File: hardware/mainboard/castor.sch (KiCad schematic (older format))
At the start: 42 parts, among them Q1 MMBT3906, U3 TL074, U4 74LVC2G74, U5 MCP6001-OT, U6 TL074

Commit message: hardware: assign new MPNs for mainboard BOM
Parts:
- C11, C12, C13: Reqs audio path, 25v -> audio path, 20v; finalized yes -> yes & alt; mpn alt (none) -> CL21A106KAFN3NE
- C14, C15, C16, C17: Reqs audio filter, 25v -> audio filter, 20v
- C9: finalized yes -> yes & alt; mpn alt GRM1885C1H102FA01D -> GRM1885C1H102FA01*
- R10, R11, R12: mpn alts 2 (none) -> RT0603DRD0747KL
- R13, R14, R15, R2, R6: mpn RR0816P-103-D -> RG1608P-103-D-T5; mpn alt ERA-3AED103V -> RR0816P-103-D; mpn alts 2 (none) -> ERA-3AED103V
- U5: mpn alt (none) -> AD8541ARTZ
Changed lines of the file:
@@
 F 3 "~" H 2500 1400 50  0001 C CNN
 F 4 "yes" H 2500 1400 50  0001 C CNN "finalized"
-F 5 "RR0816P-103-D" H 2500 1400 50  0001 C CNN "mpn"
+F 5 "RG1608P-103-D-T5" H 2500 1400 50  0001 C CNN "mpn"
 F 6 "1%, 15mW, control path" H 2500 1400 50  0001 C CNN "Reqs"
 F 7 "62mW, 0.5%" H 2500 1400 50  0001 C CNN "mpn specs"
-F 8 "ERA-3AED103V" H 2500 1400 50  0001 C CNN "mpn alt"
+F 8 "RR0816P-103-D" H 2500 1400 50  0001 C CNN "mpn alt"
+F 9 "ERA-3AED103V" H 2500 1400 50  0001 C CNN "mpn alts 2"
 	1    2500 1400
 	-1   0    0    1
@@
 F 3 "~" H 3300 2500 50  0001 C CNN
 F 4 "C0G 1%, 25v, ramp core" H 3300 2500 50  0001 C CNN "Reqs"
-F 5 "yes" H 3300 2500 50  0001 C CNN "finalized"
+F 5 "yes & alt" H 3300 2500 50  0001 C CNN "finalized"
 F 6 "GRM1885C1H102FA01J" H 3300 2500 50  0001 C CNN "mpn"
 F 7 "1%, 50v" H 3300 2500 50  0001 C CNN "mpn specs"
-F 8 "GRM1885C1H102FA01D" H 3300 2500 50  0001 C CNN "mpn alt"
+F 8 "GRM1885C1H102FA01*" H 3300 2500 50  0001 C CNN "mpn alt"
 	1    3300 2500
 	0    1    1    0
@@
 F 3 "~" H 4850 2550 50  0001 C CNN
 F 4 "yes" H 4850 2550 50  0001 C CNN "finalized"
-F 5 "RR0816P-103-D" H 4850 2550 50  0001 C CNN "mpn"
+F 5 "RG1608P-103-D-T5" H 4850 2550 50  0001 C CNN "mpn"
 F 6 "1%, 15mW, audio path" H 4850 2550 50  0001 C CNN "Reqs"
 F 7 "62mW, 0.5%" H 4850 2550 50  0001 C CNN "mpn specs"
-F 8 "ERA-3AED103V" H 4850 2550 50  0001 C CNN "mpn alt"
+F 8 "RR0816P-103-D" H 4850 2550 50  0001 C CNN "mpn alt"
+F 9 "ERA-3AED103V" H 4850 2550 50  0001 C CNN "mpn alts 2"
 	1    4850 2550
 	0    -1   -1   0
@@
 F 2 "Capacitor_SMD:C_0805_2012Metric_Pad1.15x1.40mm_HandSolder" H 7988 1400 50  0001 C CNN
 F 3 "~" H 7950 1550 50  0001 C CNN
-F 4 "yes" H 7950 1550 50  0001 C CNN "finalized"
+F 4 "yes & alt" H 7950 1550 50  0001 C CNN "finalized"
 F 5 "CL21A106KAYNNN" H 7950 1550 50  0001 C CNN "mpn"
 F 6 "10% 25v" H 7950 1550 50  0001 C CNN "mpn specs"
-F 7 "" H 7950 1550 50  0001 C CNN "mpn alt"
-F 8 "audio path, 25v" H 7950 1550 50  0001 C CNN "Reqs"
+F 7 "CL21A106KAFN3NE" H 7950 1550 50  0001 C CNN "mpn alt"
+F 8 "audio path, 20v" H 7950 1550 50  0001 C CNN "Reqs"
 	1    7950 1550
 	0    1    1    0
@@
 F 3 "~" H 8350 1550 50  0001 C CNN
 F 4 "yes" H 8350 1550 50  0001 C CNN "finalized"
-F 5 "RR0816P-103-D" H 8350 1550 50  0001 C CNN "mpn"
+F 5 "RG1608P-103-D-T5" H 8350 1550 50  0001 C CNN "mpn"
 F 6 "1%, 15mW, audio path" H 8350 1550 50  0001 C CNN "Reqs"
 F 7 "62mW, 0.5%" H 8350 1550 50  0001 C CNN "mpn specs"
-F 8 "ERA-3AED103V" H 8350 1550 50  0001 C CNN "mpn alt"
+F 8 "RR0816P-103-D" H 8350 1550 50  0001 C CNN "mpn alt"
+F 9 "ERA-3AED103V" H 8350 1550 50  0001 C CNN "mpn alts 2"
 	1    8350 1550
 	0    -1   -1   0
@@
 F 7 "62mW, 0.5%" H 8150 1700 50  0001 C CNN "mpn specs"
 F 8 "ERA-3AED473V" H 8150 1700 50  0001 C CNN "mpn alt"
+F 9 "RT0603DRD0747KL" H 8150 1700 50  0001 C CNN "mpn alts 2"
 	1    8150 1700
 	1    0    0    -1
@@
 F 6 "5% 50v" H 8850 1000 50  0001 C CNN "mpn specs"
 F 7 "GCM1885C2A220JA16J" H 8850 1000 50  0001 C CNN "mpn alt"
-F 8 "audio filter, 25v" H 8850 1000 50  0001 C CNN "Reqs"
+F 8 "audio filter, 20v" H 8850 1000 50  0001 C CNN "Reqs"
 	1    8850 1000
 	0    1    1    0
@@
 F 2 "Capacitor_SMD:C_0805_2012Metric_Pad1.15x1.40mm_HandSolder" H 7988 2550 50  0001 C CNN
 F 3 "~" H 7950 2700 50  0001 C CNN
-F 4 "yes" H 7950 2700 50  0001 C CNN "finalized"
+F 4 "yes & alt" H 7950 2700 50  0001 C CNN "finalized"
 F 5 "CL21A106KAYNNN" H 7950 2700 50  0001 C CNN "mpn"
 F 6 "10% 25v" H 7950 2700 50  0001 C CNN "mpn specs"
-F 7 "" H 7950 2700 50  0001 C CNN "mpn alt"
-F 8 "audio path, 25v" H 7950 2700 50  0001 C CNN "Reqs"
+F 7 "CL21A106KAFN3NE" H 7950 2700 50  0001 C CNN "mpn alt"
+F 8 "audio path, 20v" H 7950 2700 50  0001 C CNN "Reqs"
 	1    7950 2700
 	0    1    1    0
@@
 F 3 "~" H 8350 2700 50  0001 C CNN
 F 4 "yes" H 8350 2700 50  0001 C CNN "finalized"
-F 5 "RR0816P-103-D" H 8350 2700 50  0001 C CNN "mpn"
+F 5 "RG1608P-103-D-T5" H 8350 2700 50  0001 C CNN "mpn"
 F 6 "1%, 15mW, audio path" H 8350 2700 50  0001 C CNN "Reqs"
 F 7 "62mW, 0.5%" H 8350 2700 50  0001 C CNN "mpn specs"
-F 8 "ERA-3AED103V" H 8350 2700 50  0001 C CNN "mpn alt"
+F 8 "RR0816P-103-D" H 8350 2700 50  0001 C CNN "mpn alt"
+F 9 "ERA-3AED103V" H 8350 2700 50  0001 C CNN "mpn alts 2"
 	1    8350 2700
 	0    -1   -1   0
@@
 F 7 "62mW, 0.5%" H 8150 2850 50  0001 C CNN "mpn specs"
 F 8 "ERA-3AED473V" H 8150 2850 50  0001 C CNN "mpn alt"
+F 9 "RT0603DRD0747KL" H 8150 2850 50  0001 C CNN "mpn alts 2"
 	1    8150 2850
 	1    0    0    -1
@@
 F 6 "5% 50v" H 8850 2150 50  0001 C CNN "mpn specs"
 F 7 "GCM1885C2A220JA16J" H 8850 2150 50  0001 C CNN "mpn alt"
-F 8 "audio filter, 25v" H 8850 2150 50  0001 C CNN "Reqs"
+F 8 "audio filter, 20v" H 8850 2150 50  0001 C CNN "Reqs"
 	1    8850 2150
 	0    1    1    0
@@
 F 5 "VJ0603A8R2DXACW1BC" H 8850 4900 50  0001 C CNN "mpn"
 F 6 "25v" H 8850 4900 50  0001 C CNN "mpn specs"
-F 7 "audio filter, 25v" H 8850 4900 50  0001 C CNN "Reqs"
+F 7 "audio filter, 20v" H 8850 4900 50  0001 C CNN "Reqs"
 F 8 "GRM1885C1H8R2WA01D" H 8850 4900 50  0001 C CNN "mpn alt"
 	1    8850 4900
@@
 F 4 "yes" H 2100 5350 50  0001 C CNN "finalized"
 F 5 "MCP6001T-I/OT" H 2100 5350 50  0001 C CNN "mpn"
+F 6 "AD8541ARTZ" H 2100 5350 50  0001 C CNN "mpn alt"
 	1    2100 5350
 	1    0    0    1
@@
 F 6 "5% 50v" H 8850 3300 50  0001 C CNN "mpn specs"
 F 7 "GCM1885C2A220JA16J" H 8850 3300 50  0001 C CNN "mpn alt"
-F 8 "audio filter, 25v" H 8850 3300 50  0001 C CNN "Reqs"
+F 8 "audio filter, 20v" H 8850 3300 50  0001 C CNN "Reqs"
 	1    8850 3300
 	0    1    1    0
@@
 F 7 "62mW, 0.5%" H 8150 4000 50  0001 C CNN "mpn specs"
 F 8 "ERA-3AED473V" H 8150 4000 50  0001 C CNN "mpn alt"
+F 9 "RT0603DRD0747KL" H 8150 4000 50  0001 C CNN "mpn alts 2"
 	1    8150 4000
 	1    0    0    -1
@@
 F 3 "~" H 8350 3850 50  0001 C CNN
 F 4 "yes" H 8350 3850 50  0001 C CNN "finalized"
-F 5 "RR0816P-103-D" H 8350 3850 50  0001 C CNN "mpn"
+F 5 "RG1608P-103-D-T5" H 8350 3850 50  0001 C CNN "mpn"
 F 6 "1%, 15mW, audio path" H 8350 3850 50  0001 C CNN "Reqs"
 F 7 "62mW, 0.5%" H 8350 3850 50  0001 C CNN "mpn specs"
-F 8 "ERA-3AED103V" H 8350 3850 50  0001 C CNN "mpn alt"
+F 8 "RR0816P-103-D" H 8350 3850 50  0001 C CNN "mpn alt"
+F 9 "ERA-3AED103V" H 8350 3850 50  0001 C CNN "mpn alts 2"
 	1    8350 3850
 	0    -1   -1   0
@@
 F 2 "Capacitor_SMD:C_0805_2012Metric_Pad1.15x1.40mm_HandSolder" H 7988 3700 50  0001 C CNN
 F 3 "~" H 7950 3850 50  0001 C CNN
-F 4 "yes" H 7950 3850 50  0001 C CNN "finalized"
+F 4 "yes & alt" H 7950 3850 50  0001 C CNN "finalized"
 F 5 "CL21A106KAYNNN" H 7950 3850 50  0001 C CNN "mpn"
 F 6 "10% 25v" H 7950 3850 50  0001 C CNN "mpn specs"
-F 7 "" H 7950 3850 50  0001 C CNN "mpn alt"
-F 8 "audio path, 25v" H 7950 3850 50  0001 C CNN "Reqs"
+F 7 "CL21A106KAFN3NE" H 7950 3850 50  0001 C CNN "mpn alt"
+F 8 "audio path, 20v" H 7950 3850 50  0001 C CNN "Reqs"
 	1    7950 3850
 	0    1    1    0

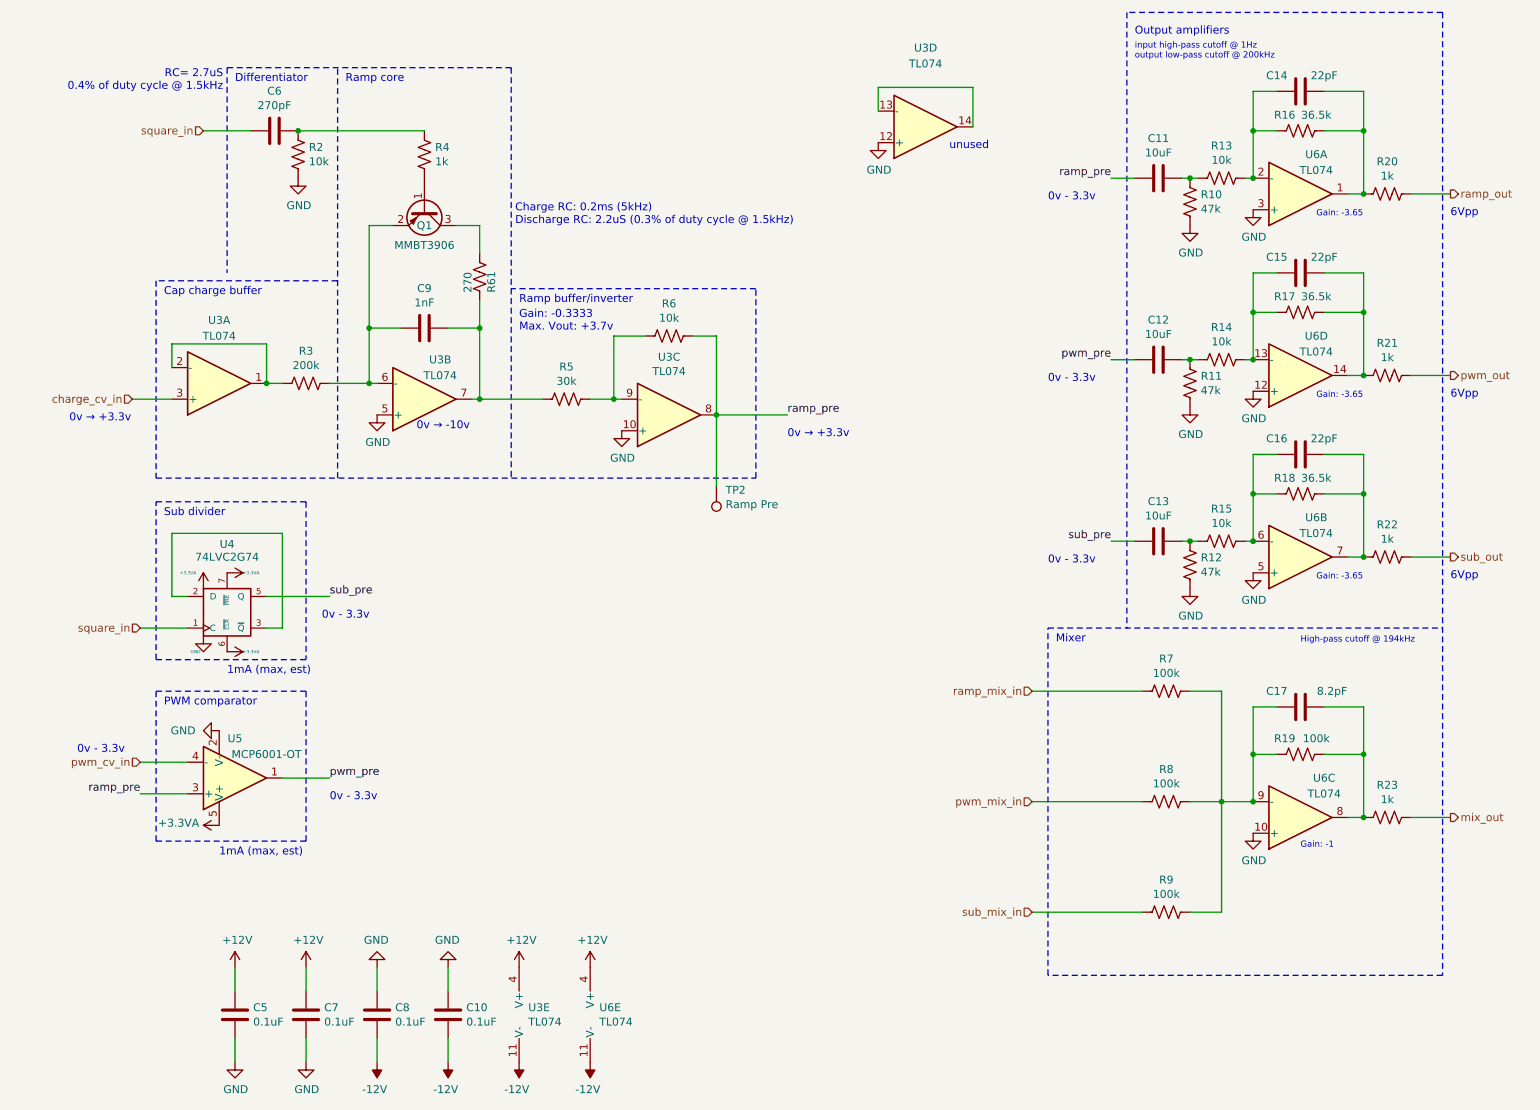
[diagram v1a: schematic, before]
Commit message: hardware: mark version 4 of the mainboard
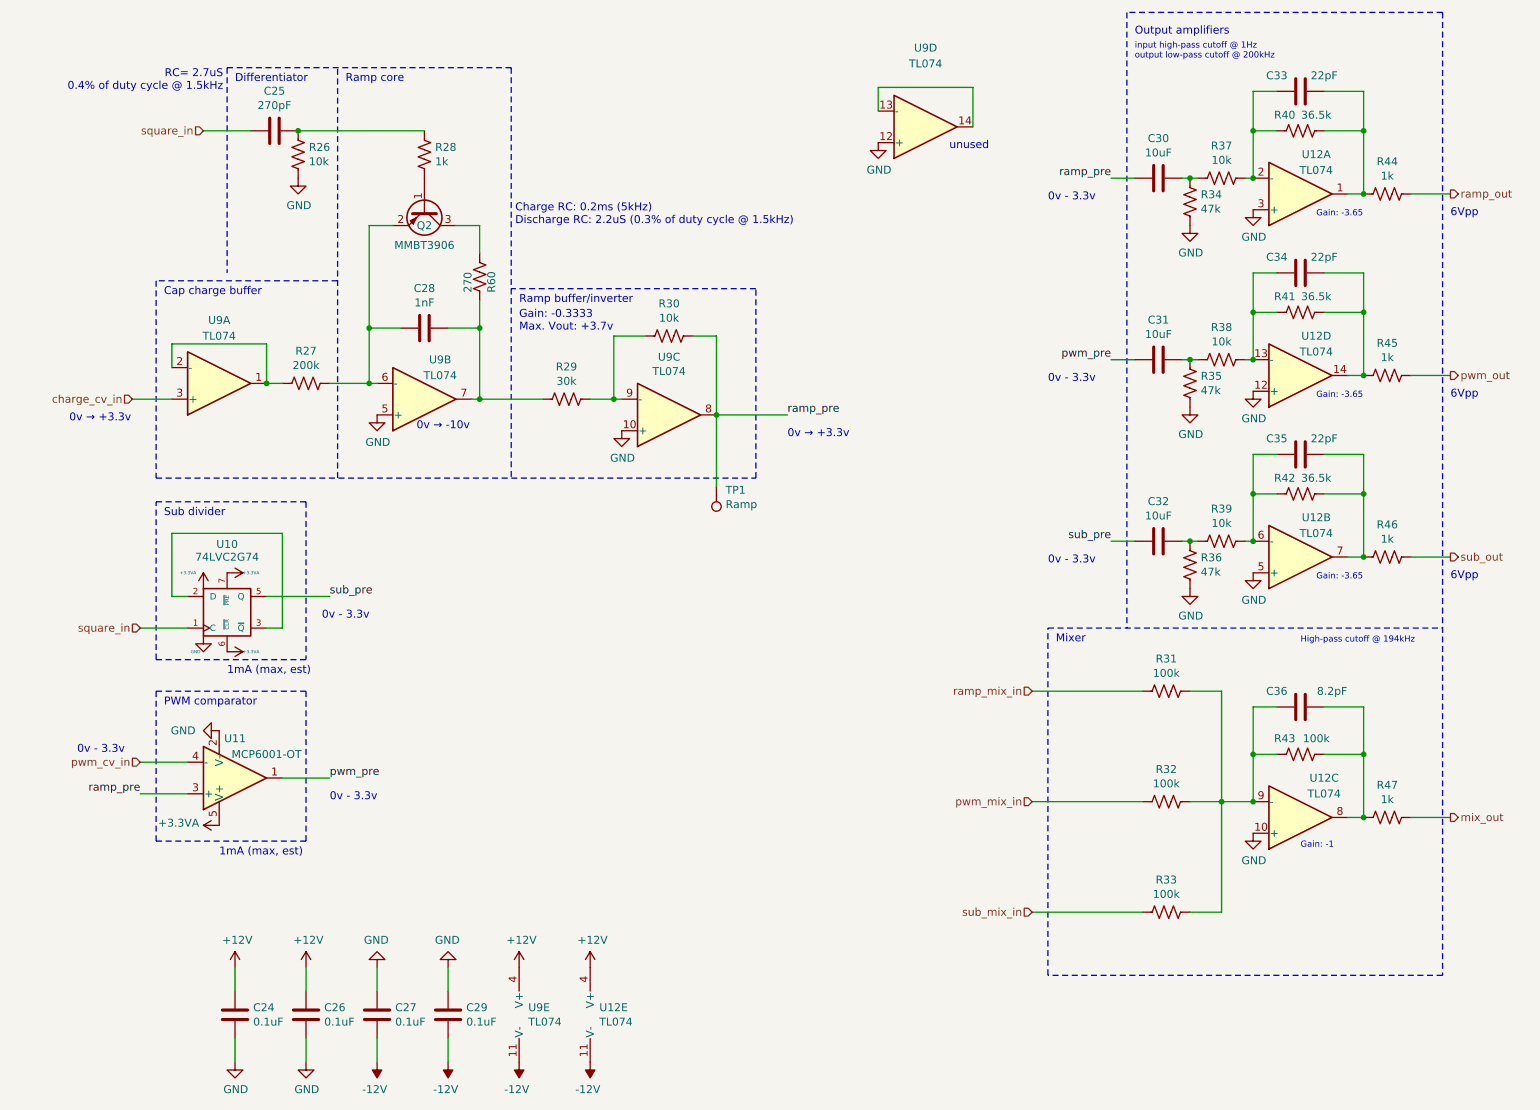
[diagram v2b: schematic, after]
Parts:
- TP2: value Ramp Pre -> Ramp
